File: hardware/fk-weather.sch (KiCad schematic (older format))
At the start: 89 parts, among them J1 MICRO-USB, J2 CONN_01X03, J3 CONN_01X06, J4 CONN_01X04, J6 CONN-HDR-2x5, M1 MOUNT_HOLE, M2 MOUNT_HOLE, M3 MOUNT_HOLE, M4 MOUNT_HOLE, Q1 2N7002LT1G, Q2 2N7002LT1G, Q3 2N7002LT1G, Q4 2N7002LT1G, SW1 SPNO, U1 ATSAMD21G18A-AU, U101 TSL2591, U102 MPL3115A2, U103 BNO055, U104 SHT31, U2 MCP1700T-XXX2E, U3 MAX4466, Y1 FC-135, Y101 FC-135

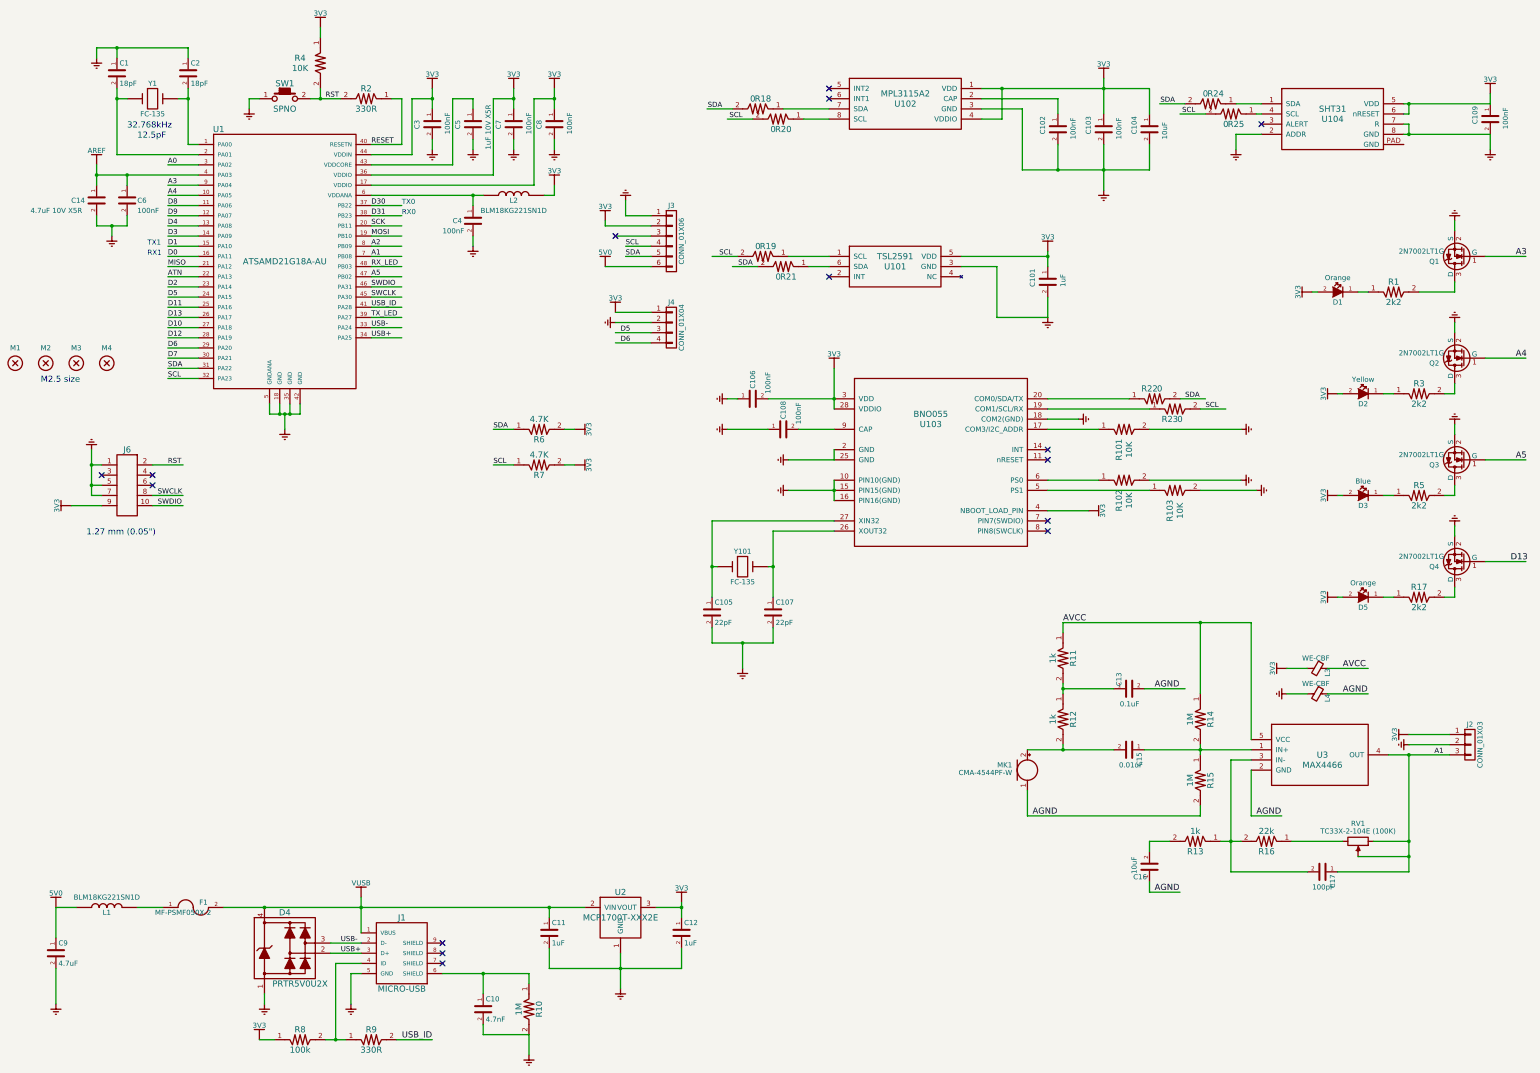
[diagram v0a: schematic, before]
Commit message: Separate I2C for BNO055, also break a third out for fk-core.
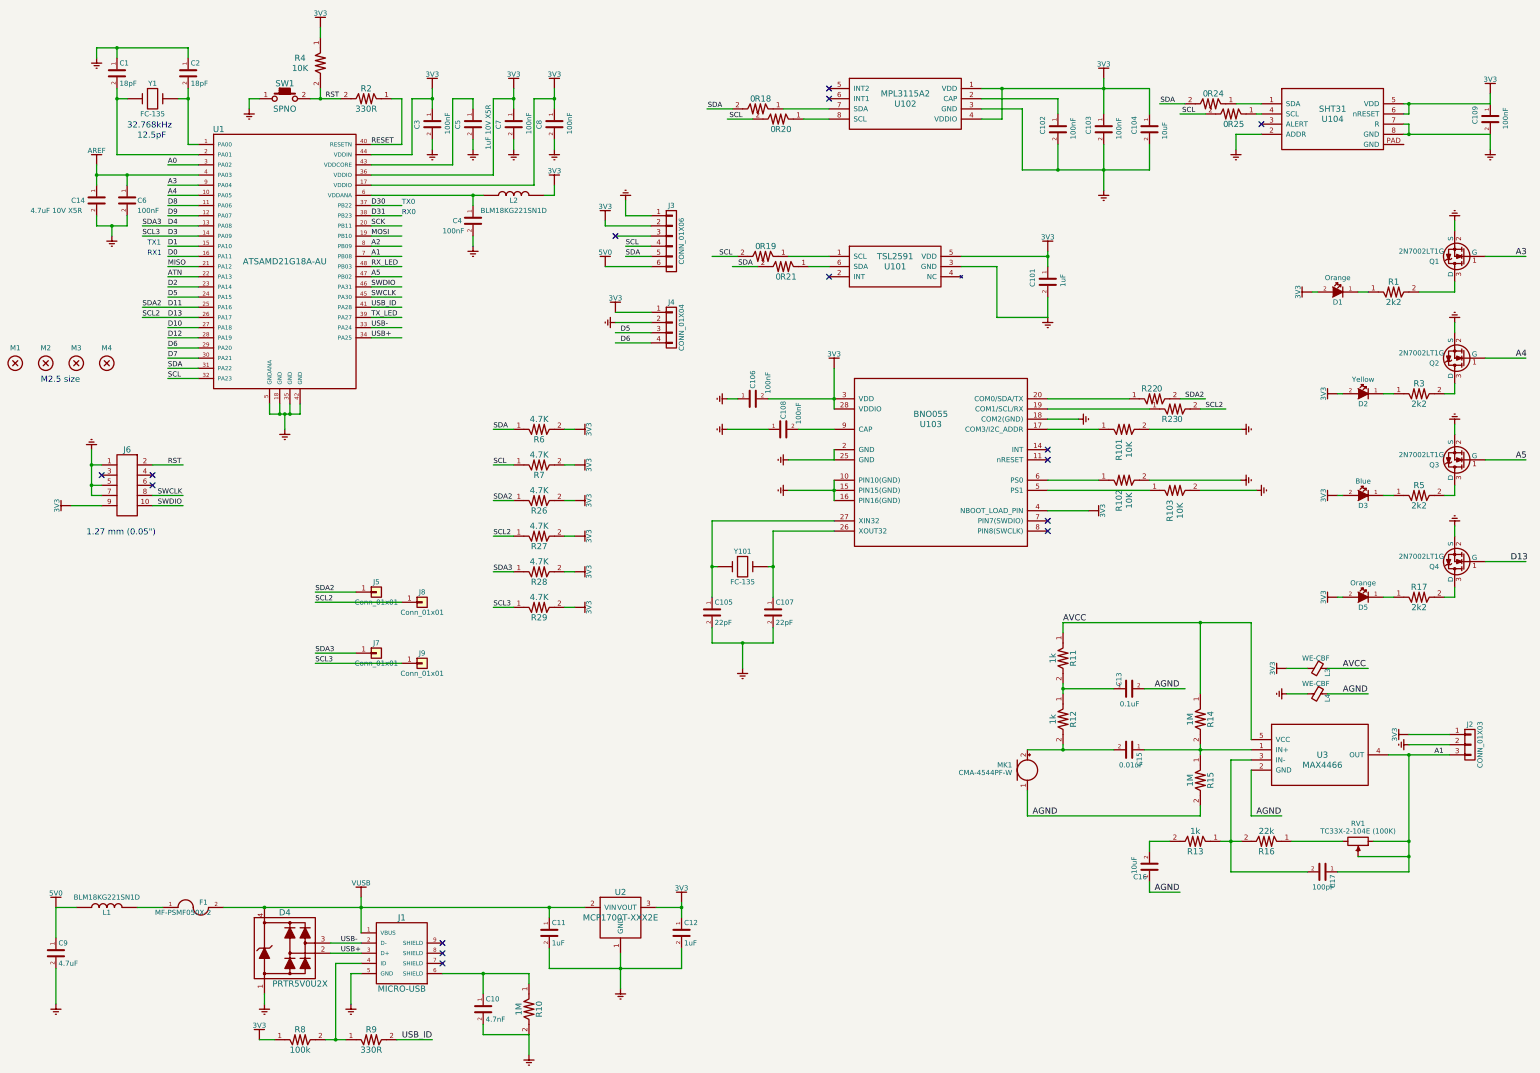
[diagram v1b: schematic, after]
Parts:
- added J5, J7, J8, J9: Conn_01x01, Measurement_Points:Measurement_Point_Round-SMD-Pad_Small, symbol Conn_01x01
- added R26, R27, R28, R29: 4.7K, Resistors_SMD:R_0603_HandSoldering, symbol RESISTOR
- L1: footprint RocketScreamKicadLibrary:IND-0603 -> Inductors_SMD:L_0603_HandSoldering
- L2: footprint RocketScreamKicadLibrary:IND-0402 -> Inductors_SMD:L_0603_HandSoldering
- MK1: footprint Socket_Strips:Socket_Strip_Angled_1x02_Pitch2.54mm -> Socket_Strips:Socket_Strip_Straight_1x02_Pitch2.54mm
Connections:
- net labels added: SCL2, SCL3, SDA2, SDA3
- wire segments 276 -> 288
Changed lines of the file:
@@
 F 0 "L2" H 5750 2400 50  0000 C CNN
 F 1 "BLM18KG221SN1D" H 5750 2300 50  0000 C CNN
-F 2 "RocketScreamKicadLibrary:IND-0402" H 5750 2300 60  0001 C CNN
+F 2 "Inductors_SMD:L_0603_HandSoldering" H 5750 2300 60  0001 C CNN
 F 3 "" V 5750 2450 60  0000 C CNN
 F 4 "0" H 5750 2500 50  0001 C CNN "price"
@@
 F 0 "L1" H 1750 9400 50  0000 C CNN
 F 1 "BLM18KG221SN1D" H 1750 9550 50  0000 C CNN
-F 2 "RocketScreamKicadLibrary:IND-0603" H 1750 9300 60  0001 C CNN
+F 2 "Inductors_SMD:L_0603_HandSoldering" H 1750 9300 60  0001 C CNN
 F 3 "" V 1750 9450 60  0000 C CNN
 F 4 "0" H 1750 9500 50  0001 C CNN "price"
@@
 F 0 "MK1" H 10650 8150 50  0000 R CNN
 F 1 "CMA-4544PF-W" H 10650 8075 50  0000 R CNN
-F 2 "Socket_Strips:Socket_Strip_Angled_1x02_Pitch2.54mm" V 10800 8200 50  0001 C CNN
+F 2 "Socket_Strips:Socket_Strip_Straight_1x02_Pitch2.54mm" V 10800 8200 50  0001 C CNN
 F 3 "" V 10800 8200 50  0001 C CNN
 F 4 "0" H 10650 8250 50  0001 C CNN "price"
@@
 SCL
 Text Label 12350 4450 0    50   ~ 0
-SDA
+SDA2
 Text Label 12550 4550 0    50   ~ 0
-SCL
+SCL2
 Text Label 15600 3050 0    60   ~ 0
 A3
@@
 	2650 2650 2350 2650
 Wire Wire Line
-	2650 2750 2350 2750
-Wire Wire Line
-	2650 2850 2350 2850
+	2100 2750 2650 2750
+Wire Wire Line
+	2100 2850 2650 2850
 Wire Wire Line
 	2650 2950 2350 2950
@@
 	2650 3450 2350 3450
 Wire Wire Line
-	2650 3550 2350 3550
+	2100 3550 2650 3550
 Wire Wire Line
 	2650 3750 2350 3750
@@
 	4350 2450 5450 2450
 Wire Wire Line
-	2350 3650 2650 3650
+	2100 3650 2650 3650
 Wire Wire Line
 	6850 2950 7100 2950
@@
 Wire Wire Line
 	7650 1600 7900 1600
+Text Label 2100 3550 0    50   ~ 0
+SDA2
+Text Label 2100 3650 0    50   ~ 0
+SCL2
+Text Label 2100 2750 0    50   ~ 0
+SDA3
+Text Label 2100 2850 0    50   ~ 0
+SCL3
+$Comp
+L 3V3 #PWR064
+U 1 1 59FC34E5
+P 6350 5450
+F 0 "#PWR064" H 6350 5300 50  0001 C CNN
+F 1 "3V3" H 6350 5590 50  0000 C CNN
+F 2 "" H 6350 5450 60  0000 C CNN
+F 3 "" H 6350 5450 60  0000 C CNN
+	1    6350 5450
+	0    1    1    0
+$EndComp
+$Comp
+L 3V3 #PWR065
+U 1 1 59FC34EB
+P 6350 5800
+F 0 "#PWR065" H 6350 5650 50  0001 C CNN
+F 1 "3V3" H 6350 5940 50  0000 C CNN
+F 2 "" H 6350 5800 60  0000 C CNN
+F 3 "" H 6350 5800 60  0000 C CNN
+	1    6350 5800
+	0    1    1    0
+$EndComp
+$Comp
+L RESISTOR R26
+U 1 1 59FC34F4
+P 6000 5450
+F 0 "R26" H 6000 5350 60  0000 C CNN
+F 1 "4.7K" H 6000 5550 60  0000 C CNN
+F 2 "Resistors_SMD:R_0603_HandSoldering" H 6000 5250 60  0001 C CNN
+F 3 "" H 6000 5450 60  0000 C CNN
+F 4 "0" H 6000 5450 50  0001 C CNN "price"
+F 5 "603-AF0603JR-074K7L" H 1500 3800 50  0001 C CNN "spn1"
+F 6 "mouser" H 1500 3800 50  0001 C CNN "supplier1"
+	1    6000 5450
+	1    0    0    -1
+$EndComp
+$Comp
+L RESISTOR R27
+U 1 1 59FC34FD
+P 6000 5800
+F 0 "R27" H 6000 5700 60  0000 C CNN
+F 1 "4.7K" H 6000 5900 60  0000 C CNN
+F 2 "Resistors_SMD:R_0603_HandSoldering" H 6000 5600 60  0001 C CNN
+F 3 "" H 6000 5800 60  0000 C CNN
+F 4 "0" H 6000 5800 50  0001 C CNN "price"
+F 5 "603-AF0603JR-074K7L" H 1500 4150 50  0001 C CNN "spn1"
+F 6 "mouser" H 1500 4150 50  0001 C CNN "supplier1"
+	1    6000 5800
+	1    0    0    -1
+$EndComp
+Text Label 5550 5450 0    50   ~ 0
+SDA2
+Text Label 5550 5800 0    50   ~ 0
+SCL2
+Wire Wire Line
+	5550 5450 5750 5450
+Wire Wire Line
+	5550 5800 5750 5800
+Wire Wire Line
+	6250 5450 6350 5450
+Wire Wire Line
+	6350 5800 6250 5800
+Text Label 3800 6450 0    50   ~ 0
+SCL2
+Text Label 3800 6350 0    50   ~ 0
+SDA2
+Text Label 3800 7050 0    50   ~ 0
+SCL3
+Text Label 3800 6950 0    50   ~ 0
+SDA3
+Wire Wire Line
+	3800 6950 4200 6950
+Wire Wire Line
+	3800 7050 4650 7050
+Wire Wire Line
+	3800 6350 4200 6350
+Wire Wire Line
+	3800 6450 4650 6450
+$Comp
+L Conn_01x01 J5
+U 1 1 59FC6B0B
+P 4400 6350
+F 0 "J5" H 4400 6450 50  0000 C CNN
+F 1 "Conn_01x01" H 4400 6250 50  0000 C CNN
+F 2 "Measurement_Points:Measurement_Point_Round-SMD-Pad_Small" H 4400 6350 50  0001 C CNN
+F 3 "" H 4400 6350 50  0001 C CNN
+	1    4400 6350
+	1    0    0    -1
+$EndComp
+$Comp
+L Conn_01x01 J8
+U 1 1 59FC6C80
+P 4850 6450
+F 0 "J8" H 4850 6550 50  0000 C CNN
+F 1 "Conn_01x01" H 4850 6350 50  0000 C CNN
+F 2 "Measurement_Points:Measurement_Point_Round-SMD-Pad_Small" H 4850 6450 50  0001 C CNN
+F 3 "" H 4850 6450 50  0001 C CNN
+	1    4850 6450
+	1    0    0    -1
+$EndComp
+$Comp
+L Conn_01x01 J7
+U 1 1 59FC6DBD
+P 4400 6950
+F 0 "J7" H 4400 7050 50  0000 C CNN
+F 1 "Conn_01x01" H 4400 6850 50  0000 C CNN
+F 2 "Measurement_Points:Measurement_Point_Round-SMD-Pad_Small" H 4400 6950 50  0001 C CNN
+F 3 "" H 4400 6950 50  0001 C CNN
+	1    4400 6950
+	1    0    0    -1
+$EndComp
+$Comp
+L Conn_01x01 J9
+U 1 1 59FC6EFD
+P 4850 7050
+F 0 "J9" H 4850 7150 50  0000 C CNN
+F 1 "Conn_01x01" H 4850 6950 50  0000 C CNN
+F 2 "Measurement_Points:Measurement_Point_Round-SMD-Pad_Small" H 4850 7050 50  0001 C CNN
+F 3 "" H 4850 7050 50  0001 C CNN
+	1    4850 7050
+	1    0    0    -1
+$EndComp
+$Comp
+L 3V3 #PWR066
+U 1 1 59FC950C
+P 6350 6150
+F 0 "#PWR066" H 6350 6000 50  0001 C CNN
+F 1 "3V3" H 6350 6290 50  0000 C CNN
+F 2 "" H 6350 6150 60  0000 C CNN
+F 3 "" H 6350 6150 60  0000 C CNN
+	1    6350 6150
+	0    1    1    0
+$EndComp
+$Comp
+L 3V3 #PWR067
+U 1 1 59FC9512
+P 6350 6500
+F 0 "#PWR067" H 6350 6350 50  0001 C CNN
+F 1 "3V3" H 6350 6640 50  0000 C CNN
+F 2 "" H 6350 6500 60  0000 C CNN
+F 3 "" H 6350 6500 60  0000 C CNN
+	1    6350 6500
+	0    1    1    0
+$EndComp
+$Comp
+L RESISTOR R28
+U 1 1 59FC951B
+P 6000 6150
+F 0 "R28" H 6000 6050 60  0000 C CNN
+F 1 "4.7K" H 6000 6250 60  0000 C CNN
+F 2 "Resistors_SMD:R_0603_HandSoldering" H 6000 5950 60  0001 C CNN
+F 3 "" H 6000 6150 60  0000 C CNN
+F 4 "0" H 6000 6150 50  0001 C CNN "price"
+F 5 "603-AF0603JR-074K7L" H 1500 4500 50  0001 C CNN "spn1"
+F 6 "mouser" H 1500 4500 50  0001 C CNN "supplier1"
+	1    6000 6150
+	1    0    0    -1
+$EndComp
+$Comp
+L RESISTOR R29
+U 1 1 59FC9524
+P 6000 6500
+F 0 "R29" H 6000 6400 60  0000 C CNN
+F 1 "4.7K" H 6000 6600 60  0000 C CNN
+F 2 "Resistors_SMD:R_0603_HandSoldering" H 6000 6300 60  0001 C CNN
+F 3 "" H 6000 6500 60  0000 C CNN
+F 4 "0" H 6000 6500 50  0001 C CNN "price"
+F 5 "603-AF0603JR-074K7L" H 1500 4850 50  0001 C CNN "spn1"
+F 6 "mouser" H 1500 4850 50  0001 C CNN "supplier1"
+	1    6000 6500
+	1    0    0    -1
+$EndComp
+Text Label 5550 6150 0    50   ~ 0
+SDA3
+Text Label 5550 6500 0    50   ~ 0
+SCL3
+Wire Wire Line
+	5550 6150 5750 6150
+Wire Wire Line
+	5550 6500 5750 6500
+Wire Wire Line
+	6250 6150 6350 6150
+Wire Wire Line
+	6350 6500 6250 6500
 $EndSCHEMATC

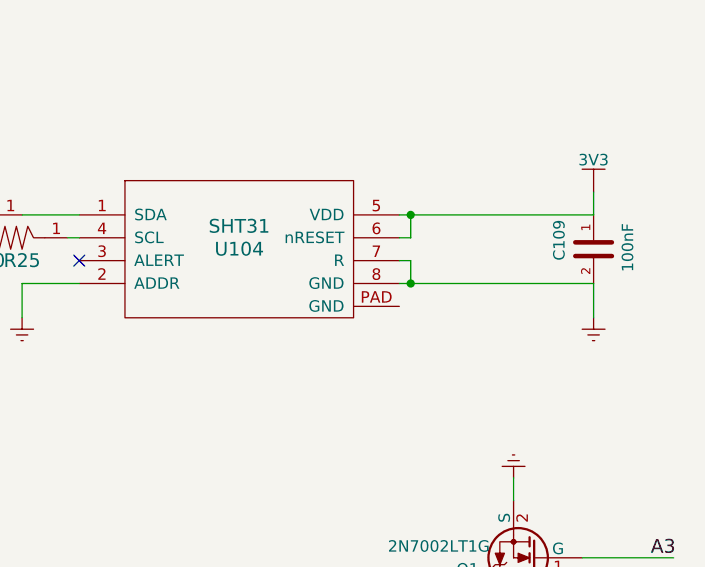
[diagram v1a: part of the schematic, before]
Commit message: Using a better SHT3x footprint.
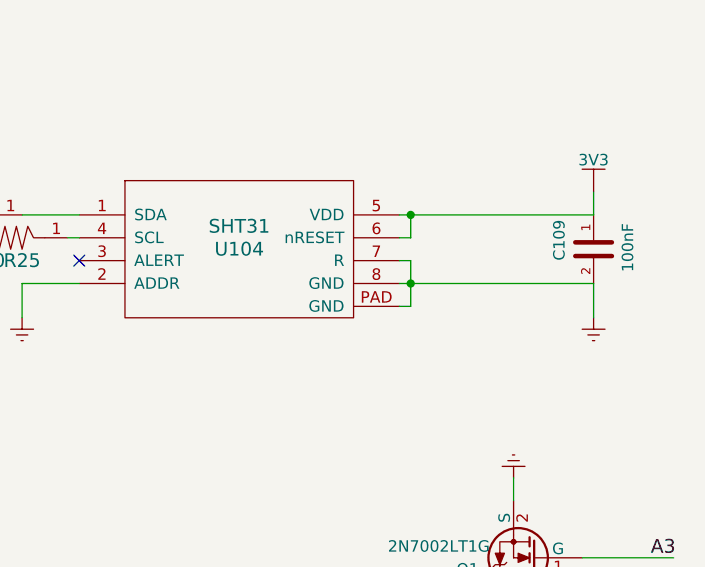
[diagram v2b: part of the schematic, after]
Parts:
- U104: footprint Housings_DFN_QFN:DFN-8_2x2mm_Pitch0.5mm -> conservify:SHT3x
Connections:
- wire segments 288 -> 289
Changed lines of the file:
@@
 F 0 "U104" H 13800 1700 60  0000 C CNN
 F 1 "SHT31" H 13800 1800 60  0000 C CNN
-F 2 "Housings_DFN_QFN:DFN-8_2x2mm_Pitch0.5mm" H 13800 1700 60  0001 C CNN
+F 2 "conservify:SHT3x" H 13800 1700 60  0001 C CNN
 F 3 "" H 13800 1700 60  0001 C CNN
 F 4 "0" H 13800 1800 50  0001 C CNN "price"
@@
 	14500 1750 14550 1750
 Wire Wire Line
-	14550 1750 14550 1850
+	14550 1750 14550 1950
 Wire Wire Line
 	14500 1850 15350 1850
@@
 Wire Wire Line
 	6350 6500 6250 6500
+Wire Wire Line
+	14550 1950 14500 1950
 $EndSCHEMATC
